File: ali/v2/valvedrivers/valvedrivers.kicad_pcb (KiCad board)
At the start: 4 copper layers, 85 x 76 mm, 152 parts, among them J1 Conn_02x01, J10 Conn_01x02, J11 Conn_01x02, J12 Conn_01x02, J13 Conn_01x02, J14 Conn_01x02, J15 Conn_01x02, J16 Conn_01x02, J17 Conn_01x02, J18 Conn_01x02, J19 Conn_01x02, J2 Conn_01x05, J20 Conn_01x02, J3 USB_C_Receptacle_USB2.0_16P, J4 Screw_Terminal_01x02, J5 Screw_Terminal_01x02, J6 Screw_Terminal_01x02, J7 Conn_01x03, J8 Vertical Ethernet, J9 Conn_01x02, SW1 SKRPANE010, U1 STM32H563RIV6, U10 PS2841-4B, U11 PS2841-4B, U12 IPS4140HQ, U13 PS2841-4B, U14 PS2841-4B, U2 LTV-816S, U3 AP2112K-3.3, U4 TJA1462ATK, U5 LAN8742AI, U6 IPS4140HQ, U7 PS2841-4B, U8 PS2841-4B, U9 IPS4140HQ, Y1 25 MHz, Y2 25 MHz

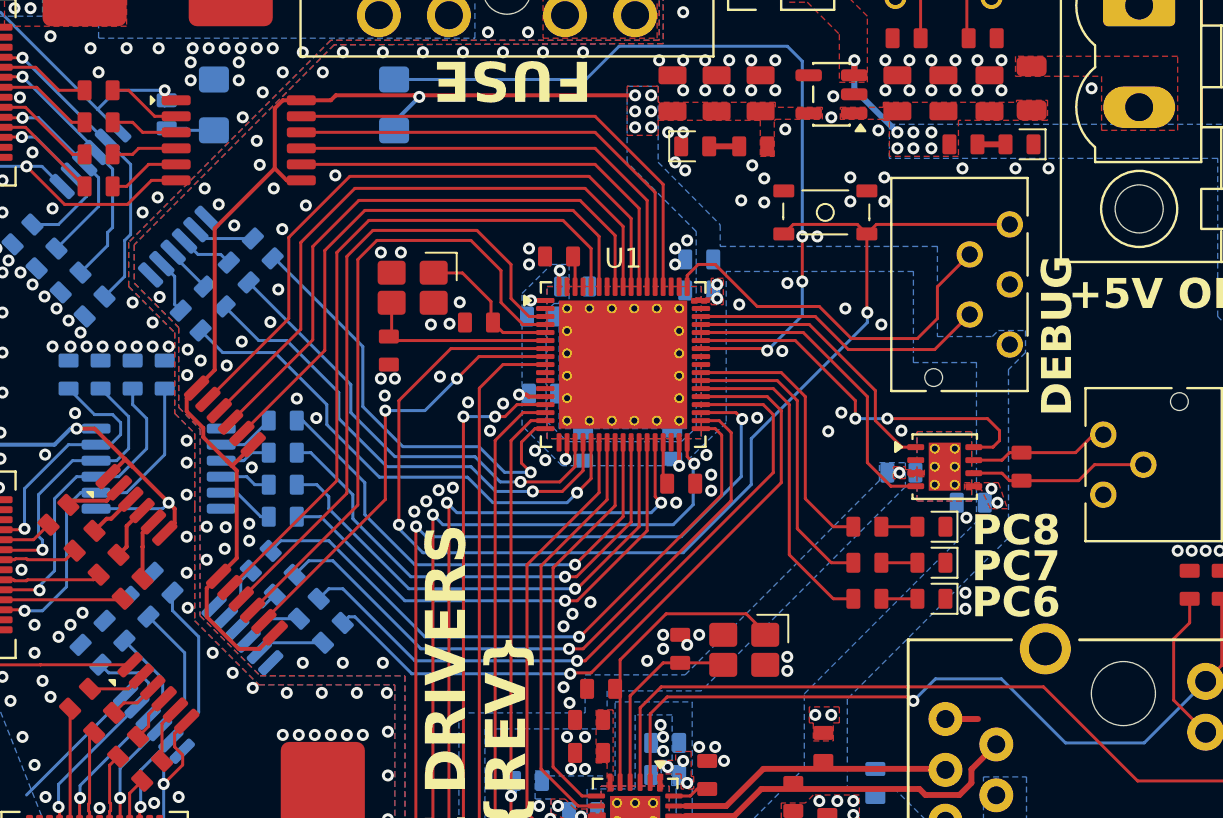
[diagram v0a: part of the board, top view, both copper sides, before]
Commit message: Globally remove LCSC labels, update MPNs and IOCs, add +5V monitoring to DAQs, fix some footprints
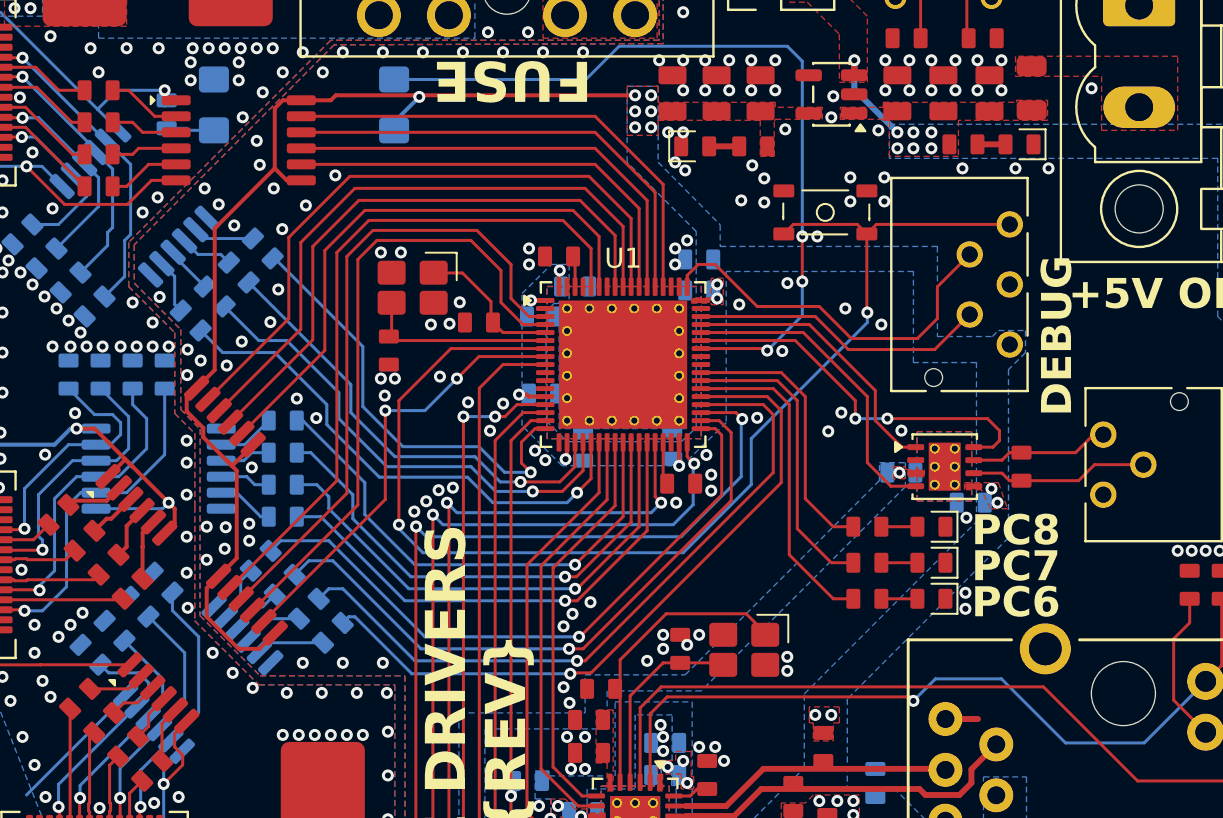
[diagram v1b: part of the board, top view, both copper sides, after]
